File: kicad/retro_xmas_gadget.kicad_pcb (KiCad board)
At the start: 2 copper layers, 66 x 86.4 mm, 18 parts, among them J1 USB_C_Receptacle_USB2.0_16P, J2 SD_Card_Receptacle, J3 AudioJack3_SwitchTR, Q1 UMH3N, SW3 SW_SPDT, U1 CP2102N-Axx-xQFN28, U2 ESP32-S3-WROOM-1

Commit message: complete most of design
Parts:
- added C10: 100nf, Capacitor_SMD:C_0603_1608Metric_Pad1.08x0.95mm_HandSolder, B.Cu at (87.0, 68.8)
- added C11: 100nf, Capacitor_SMD:C_0603_1608Metric_Pad1.08x0.95mm_HandSolder, B.Cu at (89.2, 102.4)
- added C12: 10uf, Capacitor_SMD:C_0603_1608Metric_Pad1.08x0.95mm_HandSolder, B.Cu at (52.9, 91.7)
- added C13: 10uf, Capacitor_SMD:C_0603_1608Metric_Pad1.08x0.95mm_HandSolder, B.Cu at (59.5, 91.7)
- added C14: 100nf, Capacitor_SMD:C_0603_1608Metric_Pad1.08x0.95mm_HandSolder, B.Cu at (29.1, 69.4)
- added C15: 100nf, Capacitor_SMD:C_0603_1608Metric_Pad1.08x0.95mm_HandSolder, F.Cu at (83.1, 76.7)
- added C5: 100nf, Capacitor_SMD:C_0603_1608Metric_Pad1.08x0.95mm_HandSolder, B.Cu at (69.7, 100.5)
- added C6: 100nf, Capacitor_SMD:C_0603_1608Metric_Pad1.08x0.95mm_HandSolder, B.Cu at (69.7, 91.6)
- added C9: 10uf, Capacitor_SMD:C_0603_1608Metric_Pad1.08x0.95mm_HandSolder, B.Cu at (87.0, 67.1)
- added H1: MountingHole, MountingHole:MountingHole_2.7mm_M2.5, F.Cu at (29.2, 63.5)
- added H2: MountingHole, MountingHole:MountingHole_2.7mm_M2.5, F.Cu at (97.8, 63.5)
- added H3: MountingHole, MountingHole:MountingHole_2.7mm_M2.5, F.Cu at (29.2, 148.6)
- added H4: MountingHole, MountingHole:MountingHole_2.7mm_M2.5, F.Cu at (97.8, 148.6)
- added J4: Conn_01x18, Connector_FFC-FPC:TE_1-1734839-8_1x18-1MP_P0.5mm_Horizontal, F.Cu at (79.3, 77.3)
- added J5: Conn_01x02, Connector_JST:JST_SH_SM02B-SRSS-TB_1x02-1MP_P1.00mm_Horizontal, B.Cu at (79.8, 71.8)
- added J6: Conn_01x03, Connector_JST:JST_GH_SM03B-GHS-TB_1x03-1MP_P1.25mm_Horizontal, B.Cu at (37.8, 78.2)
- added J7: Conn_01x03, Connector_PinHeader_2.54mm:PinHeader_1x03_P2.54mm_Vertical, B.Cu at (57.1, 99.1)
- added Q2: SS8050, Package_TO_SOT_SMD:SOT-23, F.Cu at (81.8, 87.4)
- added R10: 470, Resistor_SMD:R_0603_1608Metric_Pad0.98x0.95mm_HandSolder, B.Cu at (91.4, 68.0)
- added R11: 100K, Resistor_SMD:R_0603_1608Metric_Pad0.98x0.95mm_HandSolder, B.Cu at (55.8, 95.0)
- added R12: 100K, Resistor_SMD:R_0603_1608Metric_Pad0.98x0.95mm_HandSolder, B.Cu at (59.3, 95.0)
- added R13: 10k, Resistor_SMD:R_0603_1608Metric_Pad0.98x0.95mm_HandSolder, B.Cu at (51.0, 91.7)
- added R14: 2K, Resistor_SMD:R_0603_1608Metric_Pad0.98x0.95mm_HandSolder, B.Cu at (29.1, 72.9)
- added R15: 5.1k, Resistor_SMD:R_0603_1608Metric_Pad0.98x0.95mm_HandSolder, B.Cu at (43.2, 69.3)
- added R16: 1k, Resistor_SMD:R_0603_1608Metric_Pad0.98x0.95mm_HandSolder, B.Cu at (43.2, 72.9)
- added R17: 0, Capacitor_SMD:C_0402_1005Metric, B.Cu at (37.8, 90.9)
- added R18: 0, Resistor_SMD:R_0603_1608Metric_Pad0.98x0.95mm_HandSolder, F.Cu at (78.7, 87.4)
- added R19: 1K, Resistor_SMD:R_0603_1608Metric_Pad0.98x0.95mm_HandSolder, F.Cu at (84.8, 87.4)
- added R21: 10R, Resistor_SMD:R_0603_1608Metric_Pad0.98x0.95mm_HandSolder, F.Cu at (76.5, 87.4)
- added R5: 220, Resistor_SMD:R_0603_1608Metric_Pad0.98x0.95mm_HandSolder, B.Cu at (69.7, 102.4)
- added R6: 220, Resistor_SMD:R_0603_1608Metric_Pad0.98x0.95mm_HandSolder, B.Cu at (69.7, 89.7)
- added R7: 10k, Resistor_SMD:R_0603_1608Metric_Pad0.98x0.95mm_HandSolder, B.Cu at (69.7, 98.6)
- added R8: 10k, Resistor_SMD:R_0603_1608Metric_Pad0.98x0.95mm_HandSolder, B.Cu at (69.7, 93.5)
- added R9: 10k, Resistor_SMD:R_0603_1608Metric_Pad0.98x0.95mm_HandSolder, B.Cu at (91.4, 71.5)
- added SW1: RESET, Button_Switch_SMD:SW_Push_SPST_NO_Alps_SKRK, B.Cu at (65.9, 100.4)
- added SW2: BOOT, Button_Switch_SMD:SW_Push_SPST_NO_Alps_SKRK, B.Cu at (65.9, 91.4)
- added U3: ~, Package_SO:SOP-8-1EP_4.57x4.57mm_P1.27mm_EP4.57x4.45mm_ThermalVias, B.Cu at (87.0, 75.7)
- added U4: XC6210B332MR, Package_TO_SOT_SMD:SOT-23-5, B.Cu at (56.2, 91.7)
- added U5: TP4056, Package_SO:SOP-8-1EP_4.57x4.57mm_P1.27mm_EP4.57x4.45mm_ThermalVias, B.Cu at (36.1, 71.1)
- C1, C2, C3, C4, C7, C8, D1, J1, J2, J3, Q1, R1, R2, R3, R4, U1, U2: moved to B.Cu
- SW3: value SW_SPDT -> KH-SS12F23-G6; moved to B.Cu
- moved R3 55.2 mm to (41.8, 97.2), turned to 180 degrees
- moved R4 54.1 mm to (45.4, 97.2), turned to 0 degrees
- moved SW3 52.9 mm to (34.1, 57.8), turned to 0 degrees
- moved R1 52.8 mm to (35.6, 88.7), turned to 90 degrees
- moved R2 52.6 mm to (35.6, 93.2), turned to -90 degrees
- moved C4 52.0 mm to (41.1, 87.0), turned to 0 degrees
- moved C2 52.0 mm to (44.8, 87.0)
- moved C1 51.4 mm to (44.8, 88.8)
- moved C3 51.4 mm to (41.1, 88.8), turned to 0 degrees
- moved J1 51.0 mm to (28.9, 91.1), turned to 90 degrees
- moved D1 50.9 mm to (37.8, 88.1), turned to 90 degrees
- moved J2 50.4 mm to (60.0, 71.0), turned to 0 degrees
- moved U1 50.2 mm to (43.8, 92.9)
- moved C8 45.5 mm to (93.2, 102.4)
- moved U2 40.4 mm to (88.7, 91.6), turned to 90 degrees
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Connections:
- net /IO10 renamed /SD_CD
- net /IO11 renamed /SD_CMD
- net /IO13 renamed /SD_CLK
- net /IO9 renamed /SD_DAT
- J3 pad R: unconnected-(J3-PadR) -> /HJ+
- J3 pad RN: unconnected-(J3-PadRN) -> /SPK+
- J3 pad S: unconnected-(J3-PadS) -> /AUDIO-
- J3 pad T: unconnected-(J3-PadT) -> /HJ+
- J3 pad TN: unconnected-(J3-PadTN) -> /AUDIO+
- SW3 pad 2: unconnected-(SW3-B-Pad2) -> /VBAT
- SW3 pad 3: unconnected-(SW3-C-Pad3) -> /VBAT_ON
- U1 pad 7: Net-(U1-VDD) -> Net-(U1-VREGIN)
- U2 pad 15: /IO3 -> /TFT_RST
- U2 pad 20: /IO12 -> /TFT_SDI
- U2 pad 22: /IO14 -> /TFT_CS
- U2 pad 24: /IO47 -> /TFT_DC
- U2 pad 25: /IO48 -> /TFT_SCL
- U2 pad 32: /IO39 -> /TFT_LED
- U2 pad 33: /IO40 -> /AMP_DATA
- U2 pad 34: /IO41 -> /AMP_BCLK
- U2 pad 35: /IO42 -> /AMP_LRCLK
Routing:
- net VCC: track 0.00 -> 140.7 mm, vias 0 -> 3
- net GND: track 0.00 -> 68.9 mm, vias 0 -> 35
- net /RXD: track 0.00 -> 61.5 mm, vias 0 -> 2
- net VBUS: track 0.00 -> 56.2 mm
- net /TXD: track 0.00 -> 54.7 mm, vias 0 -> 2
- net /VBAT_ON: track 0.00 -> 53.3 mm
- net /IO4: track 0.00 -> 39.8 mm, vias 0 -> 2
- net /SD_DAT: track 0.00 -> 36.8 mm
- net DTR: track 0.00 -> 33.6 mm
- net /TFT_RST: track 0.00 -> 33.2 mm, vias 0 -> 1
- net RTS: track 0.00 -> 29.7 mm
- net /SD_CLK: track 0.00 -> 28.1 mm
- net /AUDIO-: track 0.00 -> 26.0 mm
- net /IO0: track 0.00 -> 24.8 mm, vias 0 -> 3
- net /HJ+: track 0.00 -> 24.1 mm
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- added copper zone on B.Cu, net GND
- added copper zone on F.Cu, net GND
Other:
- board size 66 x 86.4 mm -> 76.2 x 101.6 mm

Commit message: initial board layout
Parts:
- added SW10: SELECT, Button_Switch_SMD:SW_SPST_SKQG_WithStem, F.Cu at (76.0, 108.9)
- added SW11: START, Button_Switch_SMD:SW_SPST_SKQG_WithStem, F.Cu at (85.7, 108.6)
- added SW12: A, Button_Switch_SMD:SW_SPST_SKQG_WithStem, F.Cu at (85.3, 124.0)
- added SW13: B, Button_Switch_SMD:SW_SPST_SKQG_WithStem, F.Cu at (71.3, 128.3)
- added SW4: UP, Button_Switch_SMD:SW_SPST_SKQG_WithStem, F.Cu at (42.7, 113.4)
- added SW5: DOWN, Button_Switch_SMD:SW_SPST_SKQG_WithStem, F.Cu at (43.4, 128.3)
- added SW6: LEFT, Button_Switch_SMD:SW_SPST_SKQG_WithStem, F.Cu at (34.7, 120.8)
- added SW7: RIGHT, Button_Switch_SMD:SW_SPST_SKQG_WithStem, F.Cu at (50.0, 120.6)
- added SW8: MENU, Button_Switch_SMD:SW_SPST_SKQG_WithStem, F.Cu at (56.2, 108.6)
- added SW9: OPTION, Button_Switch_SMD:SW_SPST_SKQG_WithStem, F.Cu at (65.8, 108.6)
- moved C12 3.81 mm to (52.9, 87.9)
- moved C13 3.81 mm to (59.5, 87.9)
- moved J7 3.81 mm to (57.1, 95.2)
- moved R13 3.81 mm to (51.0, 87.9)
- moved U4 3.81 mm to (56.2, 87.9)
- moved R11 3.81 mm to (55.8, 91.2)
- moved R12 3.81 mm to (59.3, 91.2)
- moved Q1 2.77 mm to (68.9, 93.3)
- moved R5 2.77 mm to (68.9, 99.7)
- moved R6 2.77 mm to (68.9, 87.0)
- moved R7 2.77 mm to (68.9, 95.9)
- moved SW1 2.77 mm to (65.1, 97.7)
- moved SW2 2.77 mm to (65.1, 88.7)
- moved C5 2.77 mm to (68.9, 97.8)
- moved C6 2.77 mm to (68.9, 88.9)
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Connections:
- net /IO0 renamed /BOOT
- net /IO38 renamed /LED_STATUS
- net /IO4 renamed /VBAT_SENSE
- U2 pad 10: /IO17 -> /KEY_START
- U2 pad 11: /IO18 -> /KEY_MENU
- U2 pad 12: /IO8 -> /KEY_OPTION
- U2 pad 5: /IO5 -> /KEY_B
- U2 pad 6: /IO6 -> /KEY_RIGHT
- U2 pad 7: /IO7 -> /KEY_UP
- U2 pad 8: /IO15 -> /KEY_A
- U2 pad 9: /IO16 -> /KEY_SELECT
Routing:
- net /EN: track 5.74 -> 34.0 mm, vias 0 -> 3
- net VCC: track 140.7 -> 122.7 mm, vias 3 -> 5
- net /TFT_SCL: track 18.3 -> 22.2 mm
- net GND: track 68.9 -> 72.5 mm, vias 35 -> 84
- net /VBAT_SENSE: track 39.8 -> 43.1 mm
- net /TFT_DC: track 18.2 -> 21.2 mm
- net /TXD: track 54.7 -> 52.2 mm
- net /TFT_LEDK: track 15.2 -> 17.3 mm
- net /RXD: track 61.5 -> 59.8 mm
- net DTR: track 33.6 -> 31.9 mm
- net /TFT_LEDA: track 13.5 -> 15.0 mm
- net /TFT_SDI: track 22.7 -> 23.8 mm
- net /TFT_CS: track 20.2 -> 21.2 mm
- net /SD_CLK: track 28.1 -> 27.2 mm
- net RTS: track 29.7 -> 30.3 mm
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
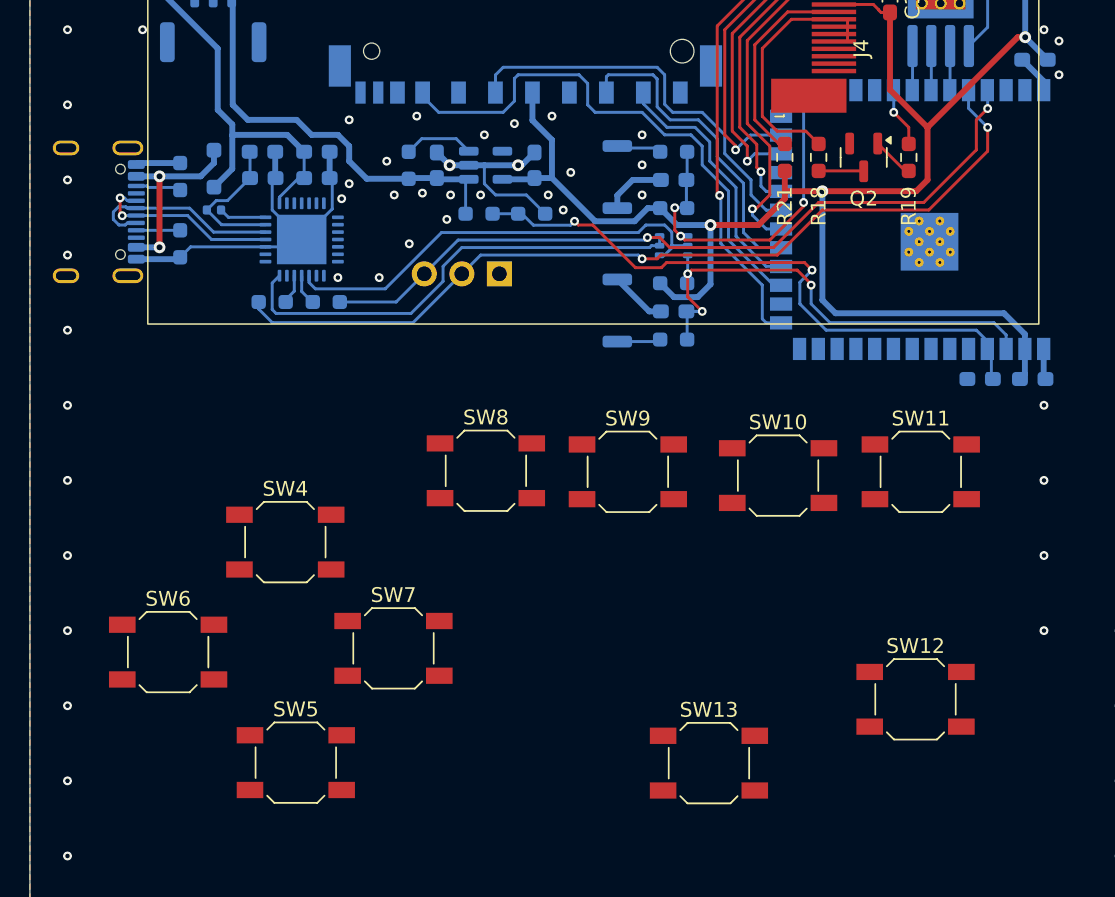
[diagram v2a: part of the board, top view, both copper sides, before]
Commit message: button positioning and routing
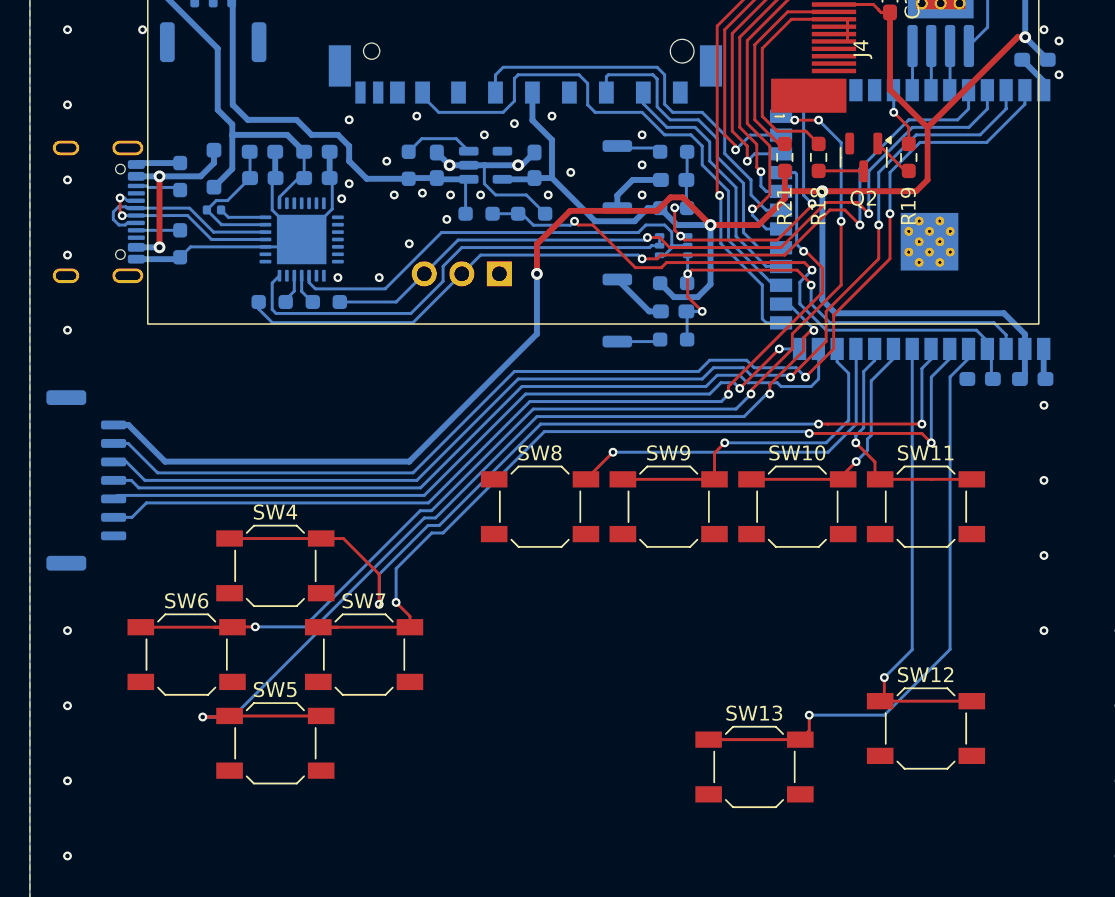
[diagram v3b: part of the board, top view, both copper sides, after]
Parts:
- added J8: Conn_01x07, Connector_JST:JST_GH_SM07B-GHS-TB_1x07-1MP_P1.25mm_Horizontal, B.Cu at (29.2, 109.2)
- moved SW8 4.40 mm to (59.9, 111.0)
- moved SW9 3.63 mm to (68.6, 111.0)
- moved SW13 3.09 mm to (74.4, 128.6)
- moved SW10 2.48 mm to (77.3, 111.0)
- moved SW11 2.39 mm to (86.0, 111.0)
- moved SW12 2.10 mm to (86.0, 126.0)
- moved SW7 2.03 mm to (48.0, 121.0)
- moved SW5 1.90 mm to (42.0, 127.0)
- moved SW4 1.74 mm to (42.0, 115.0)
- moved SW6 1.27 mm to (36.0, 121.0)
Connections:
- U2 pad 16: /IO46 -> /KEY_DOWN
- U2 pad 26: /IO45 -> /KEY_LEFT
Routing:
- net /IO1: track 0.00 -> 79.4 mm, vias 0 -> 2
- net /IO2: track 0.00 -> 78.0 mm, vias 0 -> 2
- net /KEY_LEFT: track 0.00 -> 73.6 mm, vias 0 -> 5
- net /KEY_DOWN: track 0.00 -> 64.5 mm, vias 0 -> 3
- net /IO21: track 0.00 -> 64.5 mm, vias 0 -> 2
- net /KEY_UP: track 0.00 -> 61.4 mm, vias 0 -> 3
- net /KEY_RIGHT: track 0.00 -> 59.3 mm, vias 0 -> 3
- net /IO19: track 0.00 -> 53.6 mm
- net VCC: track 122.7 -> 175.8 mm, vias 5 -> 6
- net /IO20: track 0.00 -> 50.9 mm, vias 0 -> 2
- net /KEY_B: track 0.00 -> 40.3 mm, vias 0 -> 1
- net /KEY_A: track 0.00 -> 30.9 mm, vias 0 -> 1
- net /KEY_MENU: track 0.00 -> 24.9 mm, vias 0 -> 1
- net /KEY_OPTION: track 0.00 -> 23.1 mm, vias 0 -> 1
- net /KEY_SELECT: track 0.00 -> 16.4 mm, vias 0 -> 1
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
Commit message: stitching
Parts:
- added D2: RED, LED_SMD:LED_0805_2012Metric_Pad1.15x1.40mm_HandSolder, F.Cu at (64.2, 119.3)
- added D3: GREEN, LED_SMD:LED_0805_2012Metric_Pad1.15x1.40mm_HandSolder, B.Cu at (37.1, 66.5)
- added D4: ORANGE, LED_SMD:LED_0805_2012Metric_Pad1.15x1.40mm_HandSolder, B.Cu at (37.1, 63.2)
- added R22: 1K, Resistor_SMD:R_0603_1608Metric_Pad0.98x0.95mm_HandSolder, F.Cu at (64.4, 116.5)
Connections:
- R15 pad 2: VBUS -> Net-(D3-K)
- R16 pad 1: VBUS -> Net-(D4-K)
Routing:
- net /LED_STATUS: track 0.00 -> 53.8 mm, vias 0 -> 3
- net Net-(D4-K): track 0.00 -> 13.8 mm
- net Net-(D3-K): track 0.00 -> 9.63 mm
- net VBUS: track 56.2 -> 64.7 mm
- net Net-(D2-A): track 0.00 -> 2.92 mm
- net /VBAT: track 12.7 -> 13.8 mm
- net /VBAT_ON: track 53.9 -> 54.5 mm
- net GND: vias 80 -> 133

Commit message: moar stitching
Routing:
- net GND: track 72.5 -> 73.3 mm, vias 133 -> 231
- net (no net): vias 0 -> 3

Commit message: some DRC
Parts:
- turned R14 to -90 degrees
- turned R15 to 90 degrees
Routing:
- net GND: track 73.3 -> 80.0 mm
- net VBUS: track 64.7 -> 60.1 mm
- net Net-(D3-K): track 9.63 -> 6.15 mm
- net Net-(U5-PROG): track 4.85 -> 2.90 mm, vias 2 -> 0
- net /KEY_RIGHT: track 59.3 -> 58.0 mm
- net Net-(U5-~{CHRG}): track 5.12 -> 3.82 mm, vias 2 -> 0
- net /KEY_LEFT: track 73.6 -> 72.4 mm
- net Net-(U5-~{STDBY}): track 4.02 -> 3.06 mm
- net /VBAT_ON: track 54.5 -> 53.9 mm

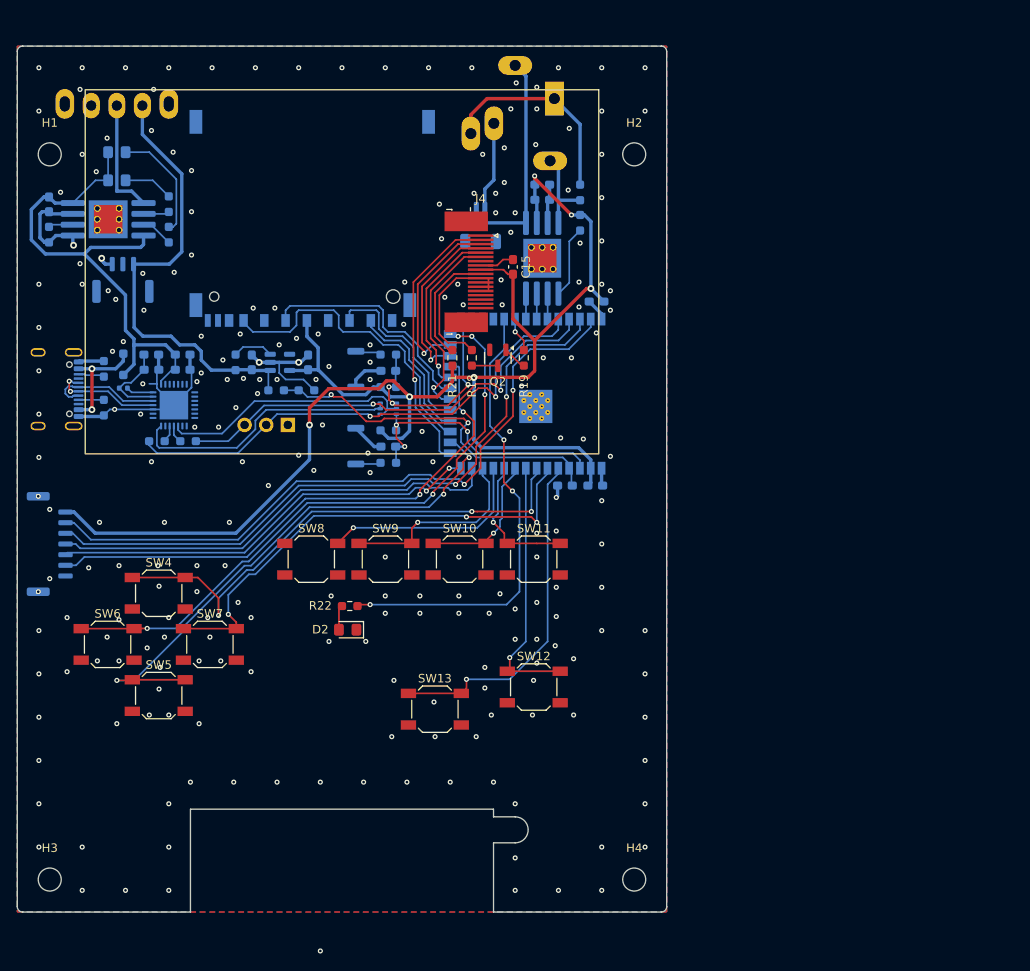
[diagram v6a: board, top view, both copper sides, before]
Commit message: change to 4 layer pcb
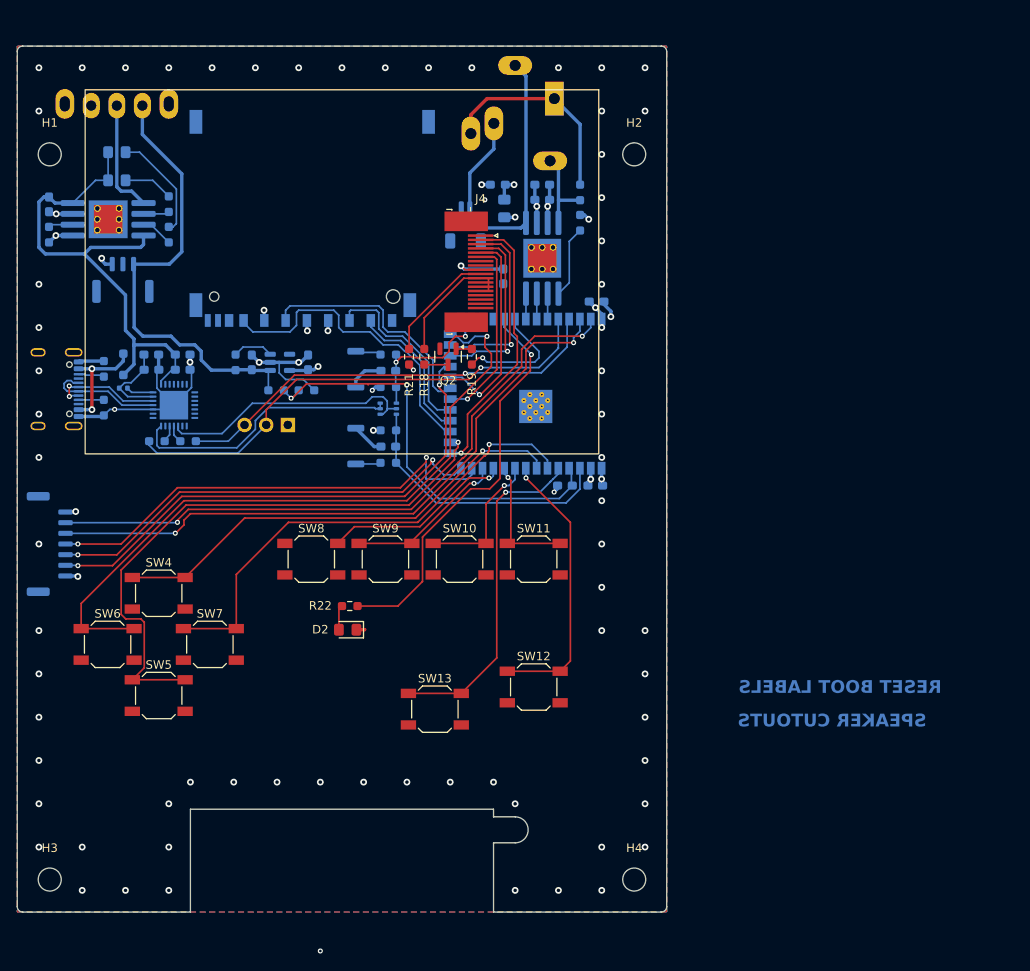
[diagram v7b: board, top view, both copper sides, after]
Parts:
- added C16: 10uf, Capacitor_SMD:C_0805_2012Metric_Pad1.18x1.45mm_HandSolder, B.Cu at (82.5, 69.8)
- added L1: L_Small, Inductor_SMD:L_0603_1608Metric_Pad1.05x0.95mm_HandSolder, B.Cu at (81.8, 67.1)
- C15: moved to B.Cu
- C9: value 10uf -> 1uf
- moved R19 6.10 mm to (78.7, 87.2), turned to 90 degrees
- moved Q2 5.84 mm to (75.9, 87.2)
- moved R18 5.59 mm to (73.2, 87.2)
- moved R21 5.08 mm to (71.4, 87.2)
- moved J5 1.77 mm to (78.0, 71.8)
- moved C15 1.60 mm to (82.4, 77.8), turned to -90 degrees
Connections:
- C10 pad 1: VCC -> VAA
- C9 pad 1: VCC -> VAA
- R9 pad 1: VCC -> VAA
- U3 pad 6: VCC -> VAA
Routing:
- net VCC: track 175.8 -> 21.8 mm, vias 6 -> 10
- net /TFT_LED: track 4.06 -> 14.3 mm
- net /KEY_LEFT: track 72.4 -> 81.2 mm, vias 5 -> 1
- net VAA: track 0.00 -> 8.64 mm, vias 0 -> 3
- net /VBAT_SENSE: track 43.1 -> 50.5 mm
- net /BOOT: track 25.4 -> 18.1 mm, vias 3 -> 2
- net /KEY_UP: track 61.4 -> 55.0 mm, vias 3 -> 1
- net /LED_STATUS: track 53.8 -> 47.5 mm, vias 3 -> 1
- net /KEY_DOWN: track 64.5 -> 69.4 mm, vias 3 -> 1
- net /KEY_OPTION: track 23.1 -> 19.0 mm
- net GND: track 80.0 -> 76.2 mm, vias 231 -> 82
- net /IO1: track 79.4 -> 75.7 mm
- net /TFT_LEDK: track 17.3 -> 13.7 mm
- net /TFT_CS: track 21.2 -> 24.1 mm
- net /IO21: track 64.5 -> 61.7 mm
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- added copper zone on In1.Cu, net GND
- added copper zone on In2.Cu, net VAA
- added copper zone on In2.Cu, net VBUS
- added copper zone on In2.Cu, net VCC
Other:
- copper layers 2 -> 4
- board text added: "RESET BOOT LABELS"
- board text added: "SPEAKER CUTOUTS"
